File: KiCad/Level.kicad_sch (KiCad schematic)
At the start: 15 parts

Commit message: PCB V1
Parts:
- U? (x3): value MT-0-102-A101-M200-RS+PJ -> MT-0-103-F001-T000-RS+PJ; symbol MT-0-102-A101-M200-RS+PJ:MT-0-102-A101-M200-RS+PJ -> MT-0-103-F001-T000-RS+PJ:MT-0-103-F001-T000-RS+PJ; LCSC C1788492 -> C1788498
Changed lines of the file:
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@@
     (stroke (width 0) (type default))
   )
-  (hierarchical_label "+3.3V" (shape input) (at 123.19 49.53 180) (fields_autoplaced)
-    (effects (font (size 1.27 1.27)) (justify right))
-  )
-  (hierarchical_label "+3.3V" (shape input) (at 125.73 87.63 180) (fields_autoplaced)
+  (hierarchical_label "+3.3V" (shape input) (at 130.81 50.8 180) (fields_autoplaced)
+    (effects (font (size 1.27 1.27)) (justify right))
+  )
+  (hierarchical_label "+3.3V" (shape input) (at 133.35 88.9 180) (fields_autoplaced)
     (effects (font (size 1.27 1.27)) (justify right))
   )
@@
     (effects (font (size 1.27 1.27)) (justify right))
   )
-  (hierarchical_label "GND" (shape input) (at 123.19 121.92 180) (fields_autoplaced)
+  (hierarchical_label "GND" (shape input) (at 130.81 120.65 180) (fields_autoplaced)
     (effects (font (size 1.27 1.27)) (justify right))
   )
@@
     (effects (font (size 1.27 1.27)) (justify right))
   )
-  (hierarchical_label "GND" (shape input) (at 125.73 85.09 180) (fields_autoplaced)
-    (effects (font (size 1.27 1.27)) (justify right))
-  )
-  (hierarchical_label "GND" (shape input) (at 123.19 46.99 180) (fields_autoplaced)
+  (hierarchical_label "GND" (shape input) (at 133.35 83.82 180) (fields_autoplaced)
+    (effects (font (size 1.27 1.27)) (justify right))
+  )
+  (hierarchical_label "GND" (shape input) (at 130.81 45.72 180) (fields_autoplaced)
     (effects (font (size 1.27 1.27)) (justify right))
   )
@@
     (effects (font (size 1.27 1.27)) (justify left))
   )
-  (hierarchical_label "+3.3V" (shape input) (at 123.19 124.46 180) (fields_autoplaced)
+  (hierarchical_label "+3.3V" (shape input) (at 130.81 125.73 180) (fields_autoplaced)
     (effects (font (size 1.27 1.27)) (justify right))
   )
@@
     )
   )
-  (symbol (lib_id "MT-0-102-A101-M200-RS+PJ:MT-0-102-A101-M200-RS+PJ") (at 130.81 46.99 0) (mirror y) (unit 1)
+  (symbol (lib_id "MT-0-103-F001-T000-RS+PJ:MT-0-103-F001-T000-RS+PJ") (at 135.89 48.26 270) (mirror x) (unit 1)
     (in_bom yes) (on_board yes) (dnp no)
-    (property "Reference" "U?" (at 132.08 41.91 0)
-      (effects (font (size 1.27 1.27)))
-    )
-    (property "Value" "MT-0-102-A101-M200-RS+PJ" (at 132.08 44.45 0)
-      (effects (font (size 1.27 1.27)))
-    )
-    (property "Footprint" "footprint:SW-TH_MT-0-103-A101-M200-RS" (at 130.81 57.15 0)
-      (effects (font (size 1.27 1.27) italic) hide)
-    )
-    (property "Datasheet" "https://item.szlcsc.com/1879284.html" (at 133.096 46.863 0)
-      (effects (font (size 1.27 1.27)) (justify left) hide)
-    )
-    (property "LCSC" "C1788492" (at 130.81 46.99 0)
+    (property "Reference" "U?" (at 140.97 49.53 0)
+      (effects (font (size 1.27 1.27)))
+    )
+    (property "Value" "MT-0-103-F001-T000-RS+PJ" (at 138.43 49.53 0)
+      (effects (font (size 1.27 1.27)))
+    )
+    (property "Footprint" "footprint:SW-TH_MT-0-103-A101-M200-RS" (at 125.73 48.26 0)
+      (effects (font (size 1.27 1.27) italic) hide)
+    )
+    (property "Datasheet" "https://item.szlcsc.com/1879284.html" (at 136.017 50.546 0)
+      (effects (font (size 1.27 1.27)) (justify left) hide)
+    )
+    (property "LCSC" "C1788498" (at 135.89 48.26 0)
       (effects (font (size 1.27 1.27)) hide)
     )
@@
     )
   )
-  (symbol (lib_id "MT-0-102-A101-M200-RS+PJ:MT-0-102-A101-M200-RS+PJ") (at 133.35 85.09 0) (mirror y) (unit 1)
+  (symbol (lib_id "MT-0-103-F001-T000-RS+PJ:MT-0-103-F001-T000-RS+PJ") (at 138.43 86.36 270) (mirror x) (unit 1)
     (in_bom yes) (on_board yes) (dnp no)
-    (property "Reference" "U?" (at 134.62 80.01 0)
-      (effects (font (size 1.27 1.27)))
-    )
-    (property "Value" "MT-0-102-A101-M200-RS+PJ" (at 134.62 82.55 0)
-      (effects (font (size 1.27 1.27)))
-    )
-    (property "Footprint" "footprint:SW-TH_MT-0-103-A101-M200-RS" (at 133.35 95.25 0)
-      (effects (font (size 1.27 1.27) italic) hide)
-    )
-    (property "Datasheet" "https://item.szlcsc.com/1879284.html" (at 135.636 84.963 0)
-      (effects (font (size 1.27 1.27)) (justify left) hide)
-    )
-    (property "LCSC" "C1788492" (at 133.35 85.09 0)
+    (property "Reference" "U?" (at 143.51 87.63 0)
+      (effects (font (size 1.27 1.27)))
+    )
+    (property "Value" "MT-0-103-F001-T000-RS+PJ" (at 140.97 87.63 0)
+      (effects (font (size 1.27 1.27)))
+    )
+    (property "Footprint" "footprint:SW-TH_MT-0-103-A101-M200-RS" (at 128.27 86.36 0)
+      (effects (font (size 1.27 1.27) italic) hide)
+    )
+    (property "Datasheet" "https://item.szlcsc.com/1879284.html" (at 138.557 88.646 0)
+      (effects (font (size 1.27 1.27)) (justify left) hide)
+    )
+    (property "LCSC" "C1788498" (at 138.43 86.36 0)
       (effects (font (size 1.27 1.27)) hide)
     )
@@
     )
   )
-  (symbol (lib_id "MT-0-102-A101-M200-RS+PJ:MT-0-102-A101-M200-RS+PJ") (at 130.81 121.92 0) (mirror y) (unit 1)
+  (symbol (lib_id "MT-0-103-F001-T000-RS+PJ:MT-0-103-F001-T000-RS+PJ") (at 135.89 123.19 270) (mirror x) (unit 1)
     (in_bom yes) (on_board yes) (dnp no)
-    (property "Reference" "U?" (at 132.08 116.84 0)
-      (effects (font (size 1.27 1.27)))
-    )
-    (property "Value" "MT-0-102-A101-M200-RS+PJ" (at 132.08 119.38 0)
-      (effects (font (size 1.27 1.27)))
-    )
-    (property "Footprint" "footprint:SW-TH_MT-0-103-A101-M200-RS" (at 130.81 132.08 0)
-      (effects (font (size 1.27 1.27) italic) hide)
-    )
-    (property "Datasheet" "https://item.szlcsc.com/1879284.html" (at 133.096 121.793 0)
-      (effects (font (size 1.27 1.27)) (justify left) hide)
-    )
-    (property "LCSC" "C1788492" (at 130.81 121.92 0)
-      (effects (font (size 1.27 1.27)) hide)
-    )
+    (property "Reference" "U?" (at 140.97 124.46 0)
+      (effects (font (size 1.27 1.27)))
+    )
+    (property "Value" "MT-0-103-F001-T000-RS+PJ" (at 138.43 124.46 0)
+      (effects (font (size 1.27 1.27)))
+    )
+    (property "Footprint" "footprint:SW-TH_MT-0-103-A101-M200-RS" (at 125.73 123.19 0)
+      (effects (font (size 1.27 1.27) italic) hide)
+    )
+    (property "Datasheet" "https://item.szlcsc.com/1879284.html" (at 136.017 125.476 0)
+      (effects (font (size 1.27 1.27)) (justify left) hide)
+    )
+    (property "LCSC" "C1788498" (at 135.89 123.19 0)
+      (effects (font (size 1.27 1.27)) hide)
+    )

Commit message: Updates for V2
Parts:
- C? (x3): value 0603B152K500NT -> CL10B102KB8NNNC; symbol 0603B152K500NT:0603B152K500NT -> CL10B102KB8NNNC:CL10B102KB8NNNC; LCSC C1595 -> C1588
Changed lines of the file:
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@@
     )
   )
-  (symbol (lib_id "0603B152K500NT:0603B152K500NT") (at 165.1 135.89 90) (unit 1)
+  (symbol (lib_id "CL10B102KB8NNNC:CL10B102KB8NNNC") (at 165.1 135.89 90) (unit 1)
     (in_bom yes) (on_board yes) (dnp no) (fields_autoplaced)
     (property "Reference" "C?" (at 168.91 134.62 90)
       (effects (font (size 1.27 1.27)) (justify right))
     )
-    (property "Value" "0603B152K500NT" (at 168.91 137.16 90)
+    (property "Value" "CL10B102KB8NNNC" (at 168.91 137.16 90)
       (effects (font (size 1.27 1.27)) (justify right))
     )
@@
       (effects (font (size 1.27 1.27)) (justify left) hide)
     )
-    (property "LCSC" "C1595" (at 165.1 135.89 0)
+    (property "LCSC" "C1588" (at 165.1 135.89 0)
       (effects (font (size 1.27 1.27)) hide)
     )
@@
     )
   )
-  (symbol (lib_id "0603B152K500NT:0603B152K500NT") (at 165.1 60.96 90) (unit 1)
+  (symbol (lib_id "CL10B102KB8NNNC:CL10B102KB8NNNC") (at 165.1 60.96 90) (unit 1)
     (in_bom yes) (on_board yes) (dnp no) (fields_autoplaced)
     (property "Reference" "C?" (at 168.91 59.69 90)
       (effects (font (size 1.27 1.27)) (justify right))
     )
-    (property "Value" "0603B152K500NT" (at 168.91 62.23 90)
+    (property "Value" "CL10B102KB8NNNC" (at 168.91 62.23 90)
       (effects (font (size 1.27 1.27)) (justify right))
     )
@@
       (effects (font (size 1.27 1.27)) (justify left) hide)
     )
-    (property "LCSC" "C1595" (at 165.1 60.96 0)
+    (property "LCSC" "C1588" (at 165.1 60.96 0)
       (effects (font (size 1.27 1.27)) hide)
     )
@@
     )
   )
-  (symbol (lib_id "0603B152K500NT:0603B152K500NT") (at 167.64 99.06 90) (unit 1)
+  (symbol (lib_id "CL10B102KB8NNNC:CL10B102KB8NNNC") (at 167.64 99.06 90) (unit 1)
     (in_bom yes) (on_board yes) (dnp no) (fields_autoplaced)
     (property "Reference" "C?" (at 171.45 97.79 90)
       (effects (font (size 1.27 1.27)) (justify right))
     )
-    (property "Value" "0603B152K500NT" (at 171.45 100.33 90)
+    (property "Value" "CL10B102KB8NNNC" (at 171.45 100.33 90)
       (effects (font (size 1.27 1.27)) (justify right))
     )
@@
       (effects (font (size 1.27 1.27)) (justify left) hide)
     )
-    (property "LCSC" "C1595" (at 167.64 99.06 0)
-      (effects (font (size 1.27 1.27)) hide)
-    )
+    (property "LCSC" "C1588" (at 167.64 99.06 0)
+      (effects (font (size 1.27 1.27)) hide)
+    )

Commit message: First production
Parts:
- gave numbers to parts that had none: 15

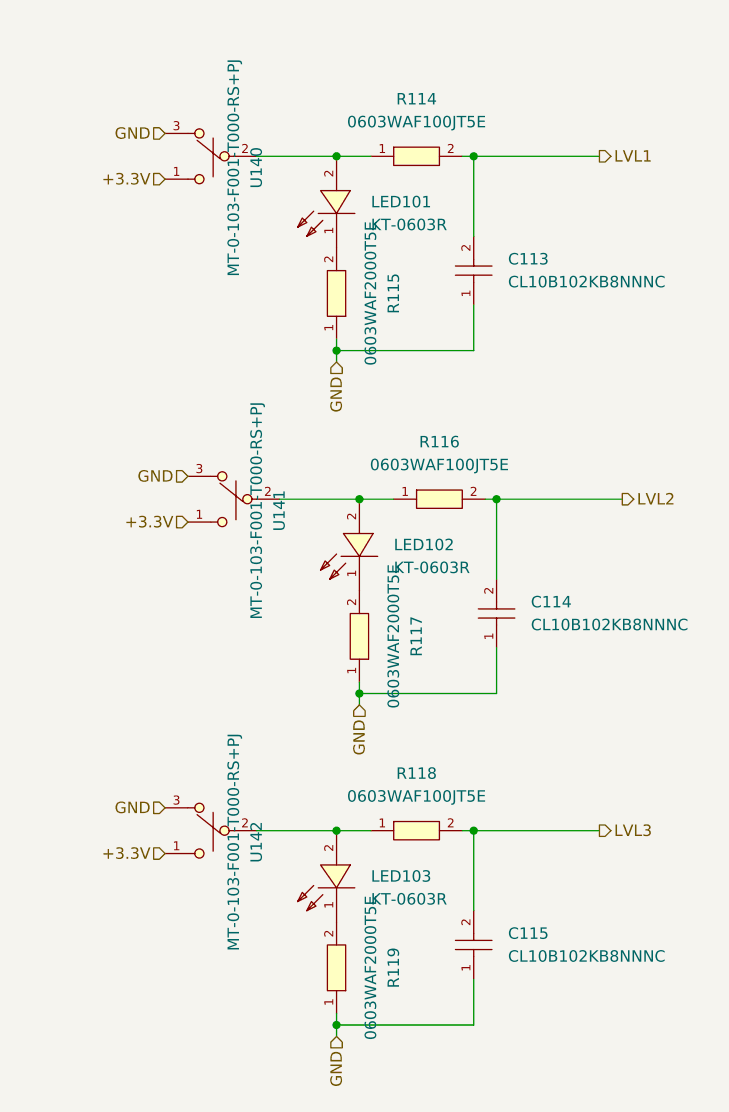
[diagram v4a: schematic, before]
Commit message: Ready for PCB layout with discreet LEDs
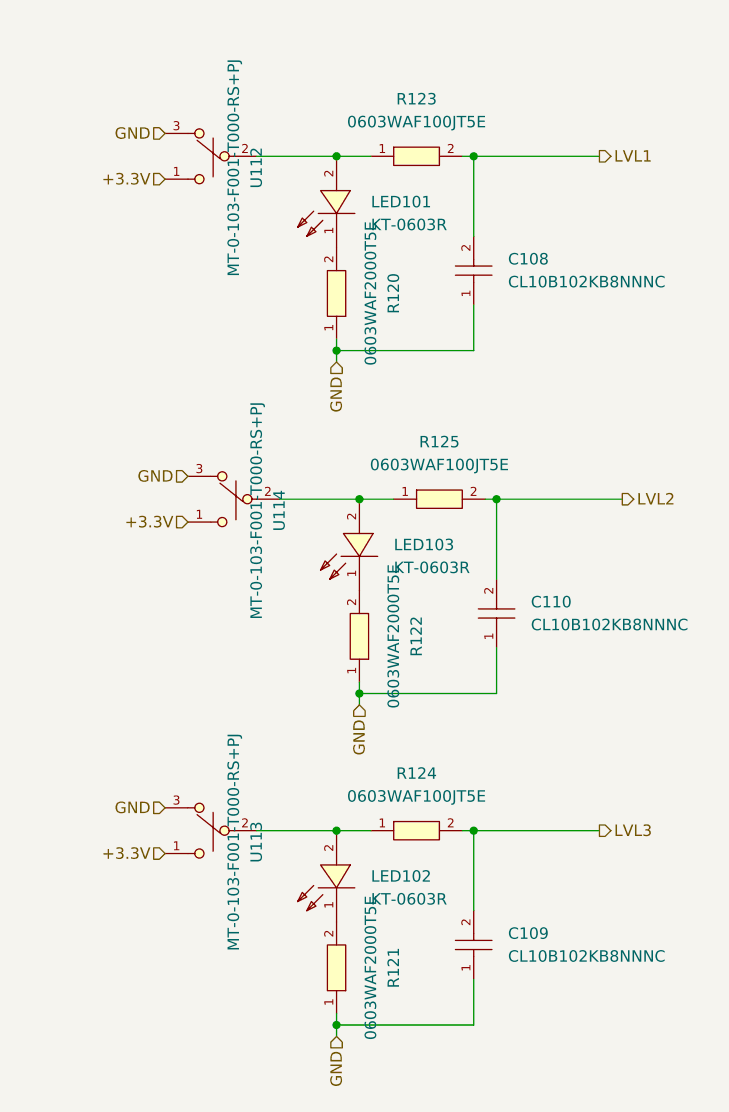
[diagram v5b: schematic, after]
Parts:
- renumbered C113 to C108, C115 to C109, C114 to C110, LED103 to LED102, LED102 to LED103, R115 to R120, R119 to R121, R117 to R122, R114 to R123, R118 to R124, R116 to R125, U140 to U112, U142 to U113, U141 to U114
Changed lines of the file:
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@@
 		(dnp no)
 		(fields_autoplaced yes)
-		(property "Reference" "R118"
+		(property "Reference" "R124"
 			(at 158.75 116.84 0)
 			(effects
@@
 			(project "Kaboom_box"
 				(path "/8d340784-229e-46d1-990c-7f8852f9fc49/d111de2c-3c3c-486e-8c4b-bd3963817676/246166fa-6b2c-4746-ad4c-b0b5fe6ecb14"
-					(reference "R118")
+					(reference "R124")
 					(unit 1)
 				)
@@
 		(on_board yes)
 		(dnp no)
-		(property "Reference" "R115"
+		(property "Reference" "R120"
 			(at 156.21 63.5 0)
 			(effects
@@
 			(project "Kaboom_box"
 				(path "/8d340784-229e-46d1-990c-7f8852f9fc49/d111de2c-3c3c-486e-8c4b-bd3963817676/246166fa-6b2c-4746-ad4c-b0b5fe6ecb14"
-					(reference "R115")
+					(reference "R120")
 					(unit 1)
 				)
@@
 		(dnp no)
 		(fields_autoplaced yes)
-		(property "Reference" "LED103"
+		(property "Reference" "LED102"
 			(at 153.67 128.27 90)
 			(effects
@@
 			(project "Kaboom_box"
 				(path "/8d340784-229e-46d1-990c-7f8852f9fc49/d111de2c-3c3c-486e-8c4b-bd3963817676/246166fa-6b2c-4746-ad4c-b0b5fe6ecb14"
-					(reference "LED103")
+					(reference "LED102")
 					(unit 1)
 				)
@@
 		(dnp no)
 		(fields_autoplaced yes)
-		(property "Reference" "C115"
+		(property "Reference" "C109"
 			(at 168.91 134.62 90)
 			(effects
@@
 			(project "Kaboom_box"
 				(path "/8d340784-229e-46d1-990c-7f8852f9fc49/d111de2c-3c3c-486e-8c4b-bd3963817676/246166fa-6b2c-4746-ad4c-b0b5fe6ecb14"
-					(reference "C115")
+					(reference "C109")
 					(unit 1)
 				)
@@
 		(on_board yes)
 		(dnp no)
-		(property "Reference" "U140"
+		(property "Reference" "U112"
 			(at 140.97 49.53 0)
 			(effects
@@
 			(project "Kaboom_box"
 				(path "/8d340784-229e-46d1-990c-7f8852f9fc49/d111de2c-3c3c-486e-8c4b-bd3963817676/246166fa-6b2c-4746-ad4c-b0b5fe6ecb14"
-					(reference "U140")
+					(reference "U112")
 					(unit 1)
 				)
@@
 		(on_board yes)
 		(dnp no)
-		(property "Reference" "U141"
+		(property "Reference" "U114"
 			(at 143.51 87.63 0)
 			(effects
@@
 			(project "Kaboom_box"
 				(path "/8d340784-229e-46d1-990c-7f8852f9fc49/d111de2c-3c3c-486e-8c4b-bd3963817676/246166fa-6b2c-4746-ad4c-b0b5fe6ecb14"
-					(reference "U141")
+					(reference "U114")
 					(unit 1)
 				)
@@
 		(dnp no)
 		(fields_autoplaced yes)
-		(property "Reference" "R114"
+		(property "Reference" "R123"
 			(at 158.75 41.91 0)
 			(effects
@@
 			(project "Kaboom_box"
 				(path "/8d340784-229e-46d1-990c-7f8852f9fc49/d111de2c-3c3c-486e-8c4b-bd3963817676/246166fa-6b2c-4746-ad4c-b0b5fe6ecb14"
-					(reference "R114")
+					(reference "R123")
 					(unit 1)
 				)
@@
 		(dnp no)
 		(fields_autoplaced yes)
-		(property "Reference" "R116"
+		(property "Reference" "R125"
 			(at 161.29 80.01 0)
 			(effects
@@
 			(project "Kaboom_box"
 				(path "/8d340784-229e-46d1-990c-7f8852f9fc49/d111de2c-3c3c-486e-8c4b-bd3963817676/246166fa-6b2c-4746-ad4c-b0b5fe6ecb14"
-					(reference "R116")
+					(reference "R125")
 					(unit 1)
 				)
@@
 		(dnp no)
 		(fields_autoplaced yes)
-		(property "Reference" "C113"
+		(property "Reference" "C108"
 			(at 168.91 59.69 90)
 			(effects
@@
 			(project "Kaboom_box"
 				(path "/8d340784-229e-46d1-990c-7f8852f9fc49/d111de2c-3c3c-486e-8c4b-bd3963817676/246166fa-6b2c-4746-ad4c-b0b5fe6ecb14"
-					(reference "C113")
+					(reference "C108")
 					(unit 1)
 				)
@@
 		(on_board yes)
 		(dnp no)
-		(property "Reference" "U142"
+		(property "Reference" "U113"
 			(at 140.97 124.46 0)
 			(effects
@@
 			(project "Kaboom_box"
 				(path "/8d340784-229e-46d1-990c-7f8852f9fc49/d111de2c-3c3c-486e-8c4b-bd3963817676/246166fa-6b2c-4746-ad4c-b0b5fe6ecb14"
-					(reference "U142")
+					(reference "U113")
 					(unit 1)
 				)
@@
 		(on_board yes)
 		(dnp no)
-		(property "Reference" "R117"
+		(property "Reference" "R122"
 			(at 158.75 101.6 0)
 			(effects
@@
 			(project "Kaboom_box"
 				(path "/8d340784-229e-46d1-990c-7f8852f9fc49/d111de2c-3c3c-486e-8c4b-bd3963817676/246166fa-6b2c-4746-ad4c-b0b5fe6ecb14"
-					(reference "R117")
+					(reference "R122")
 					(unit 1)
 				)
@@
 		(dnp no)
 		(fields_autoplaced yes)
-		(property "Reference" "LED102"
+		(property "Reference" "LED103"
 			(at 156.21 91.44 90)
 			(effects
@@
 			(project "Kaboom_box"
 				(path "/8d340784-229e-46d1-990c-7f8852f9fc49/d111de2c-3c3c-486e-8c4b-bd3963817676/246166fa-6b2c-4746-ad4c-b0b5fe6ecb14"
-					(reference "LED102")
+					(reference "LED103")
 					(unit 1)
 				)
@@
 		(on_board yes)
 		(dnp no)
-		(property "Reference" "R119"
+		(property "Reference" "R121"
 			(at 156.21 138.43 0)
 			(effects
@@
 			(project "Kaboom_box"
 				(path "/8d340784-229e-46d1-990c-7f8852f9fc49/d111de2c-3c3c-486e-8c4b-bd3963817676/246166fa-6b2c-4746-ad4c-b0b5fe6ecb14"
-					(reference "R119")
+					(reference "R121")
 					(unit 1)
 				)
@@
 		(dnp no)
 		(fields_autoplaced yes)
-		(property "Reference" "C114"
+		(property "Reference" "C110"
 			(at 171.45 97.79 90)
 			(effects
@@
 			(project "Kaboom_box"
 				(path "/8d340784-229e-46d1-990c-7f8852f9fc49/d111de2c-3c3c-486e-8c4b-bd3963817676/246166fa-6b2c-4746-ad4c-b0b5fe6ecb14"
-					(reference "C114")
-					(unit 1)
-				)
+					(reference "C110")
+					(unit 1)
+				)
